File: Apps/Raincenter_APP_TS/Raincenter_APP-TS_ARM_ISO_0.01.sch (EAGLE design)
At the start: 26 parts

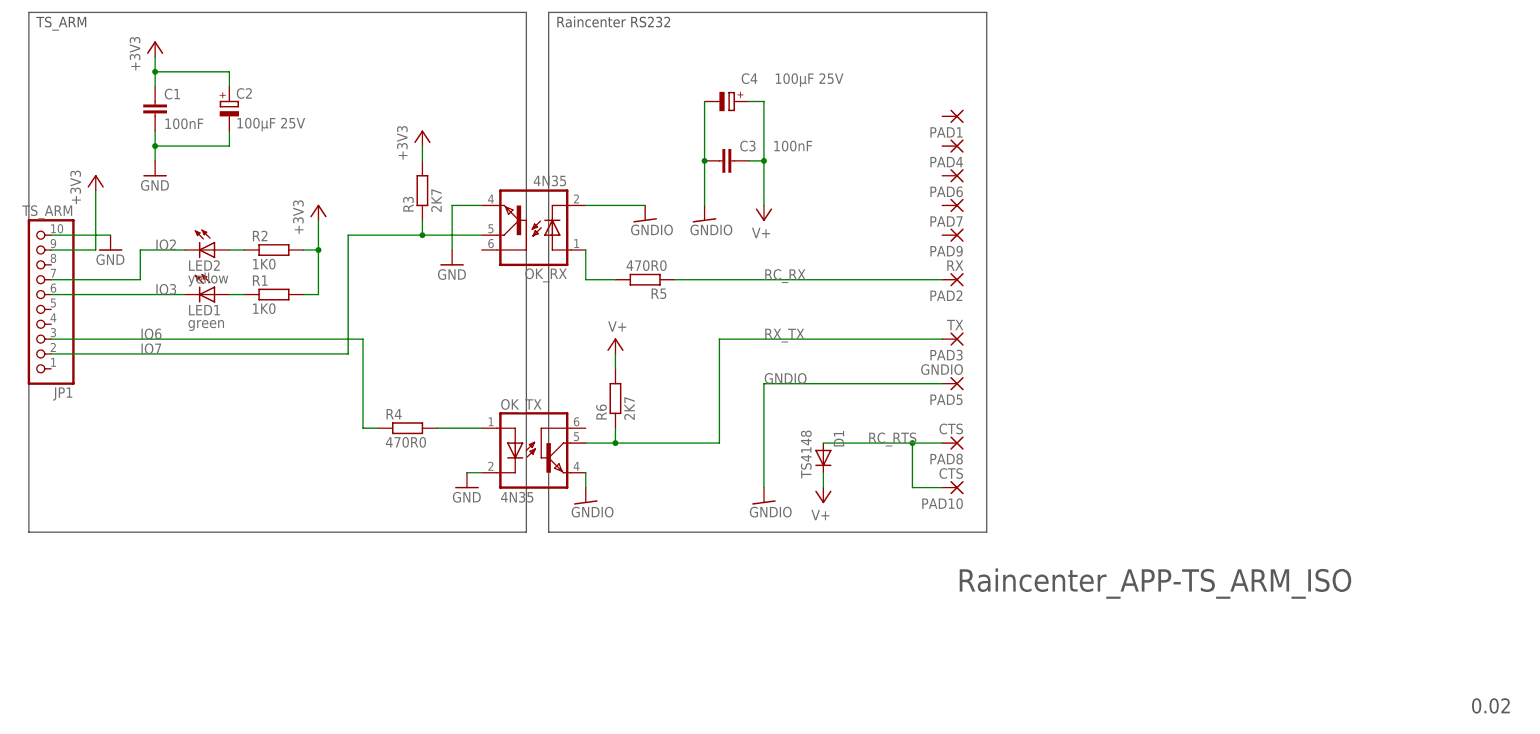
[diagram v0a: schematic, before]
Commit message: Raincenter_APP: restored Ver. 0.01, changed wire width from 16mil to 24mil
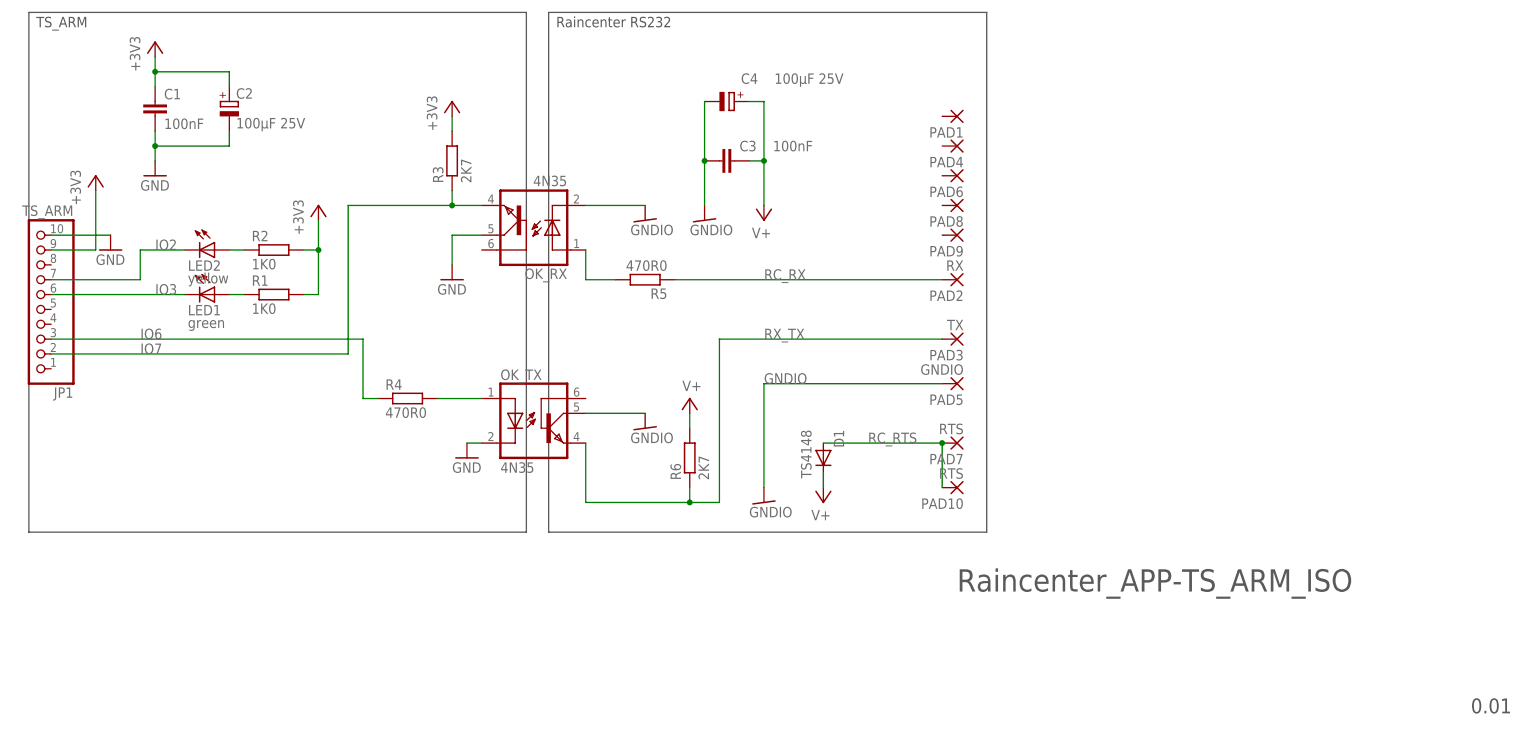
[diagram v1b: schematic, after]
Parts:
- PAD10: value CTS -> RTS
- PAD7: value WIREPADSMD1,27-254 -> RTS
- PAD8: value CTS -> WIREPADSMD1,27-254
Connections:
- net GND: now also OK_RX.COL; no longer OK_RX.EMI
- net GNDIO: now also OK_TX.COL; no longer OK_TX.EMI
- net IO7: now also OK_RX.EMI; no longer OK_RX.COL
- net RC_RTS: now also PAD7.P; no longer PAD8.P
- net RX_TX: now also OK_TX.EMI; no longer OK_TX.COL
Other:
- note added: "0.01"
- note removed: "0.02"
- moved on the sheet: OK_TX, PAD7, PAD8, R3, R4, R6
